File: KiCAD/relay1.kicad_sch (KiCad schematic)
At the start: 15 parts, among them K1 SANYOU_SRD_Form_C, K2 SANYOU_SRD_Form_C, Q2 UMH3N, Q3 MMBT3906, Q4 MMBT3906

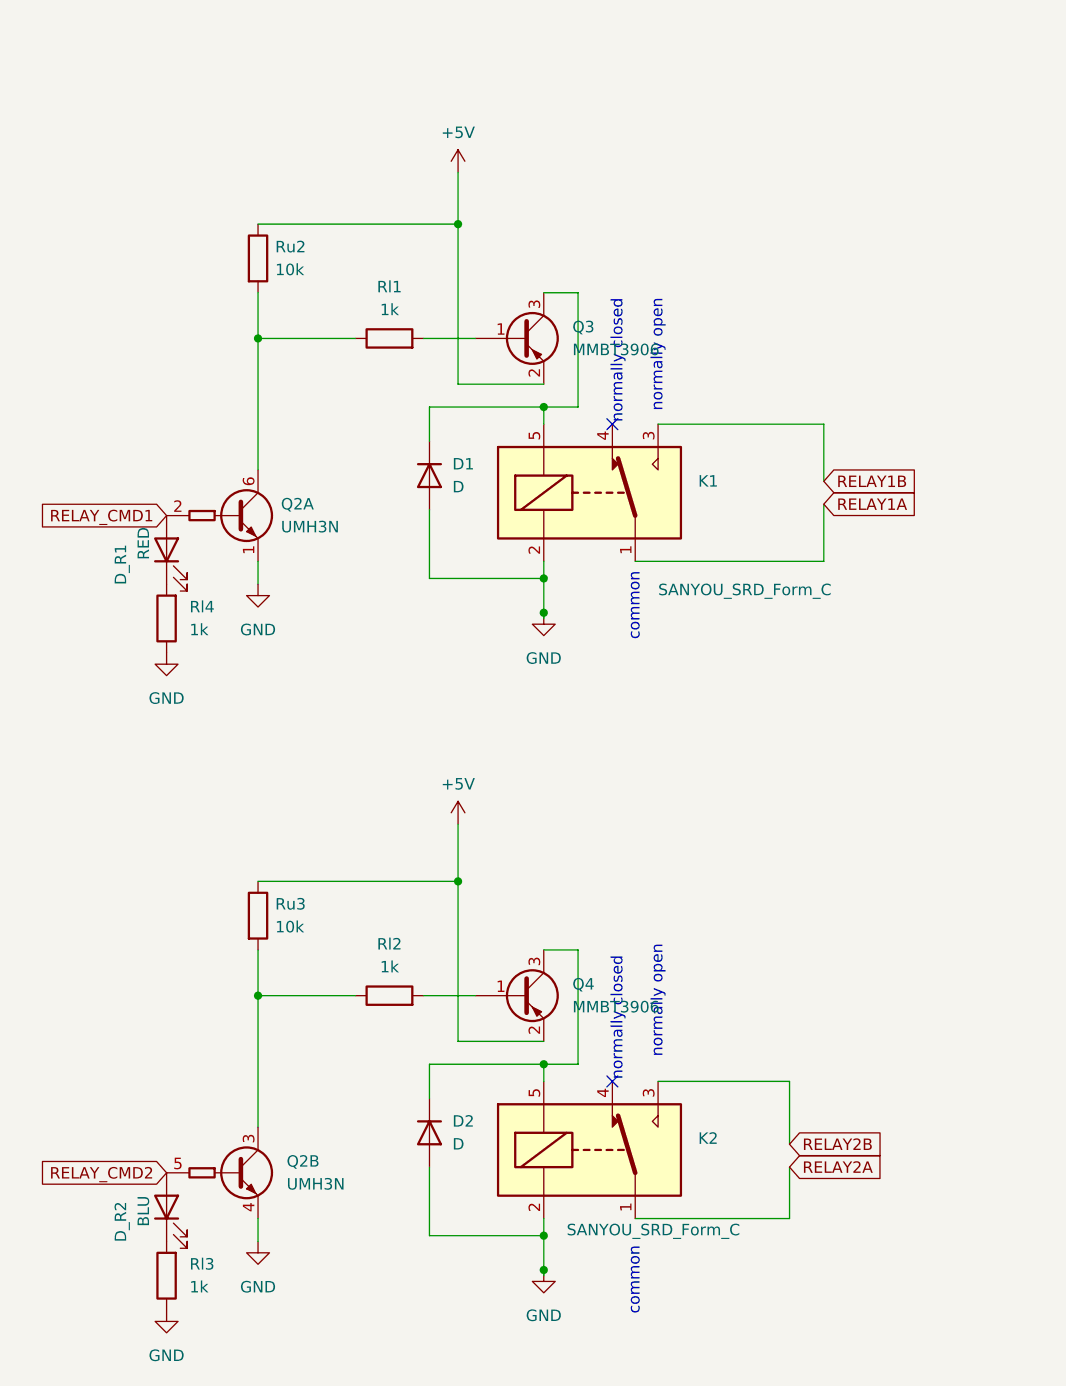
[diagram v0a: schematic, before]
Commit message: four-sonar board (#25)
The four-sonar board written about in [Dual Sonar ESP32 Garage State
Estimation](https://selectiveappeal.org/posts/garage133-dual-sonar/).

- Board supports front and back sonars for both right and left garage
bays.
- Software update for dual-observation hmm, training update.
  - Distinct states for door open with car present and not present.
- Updated ebox design, sencil fixture
- Updated device web interface
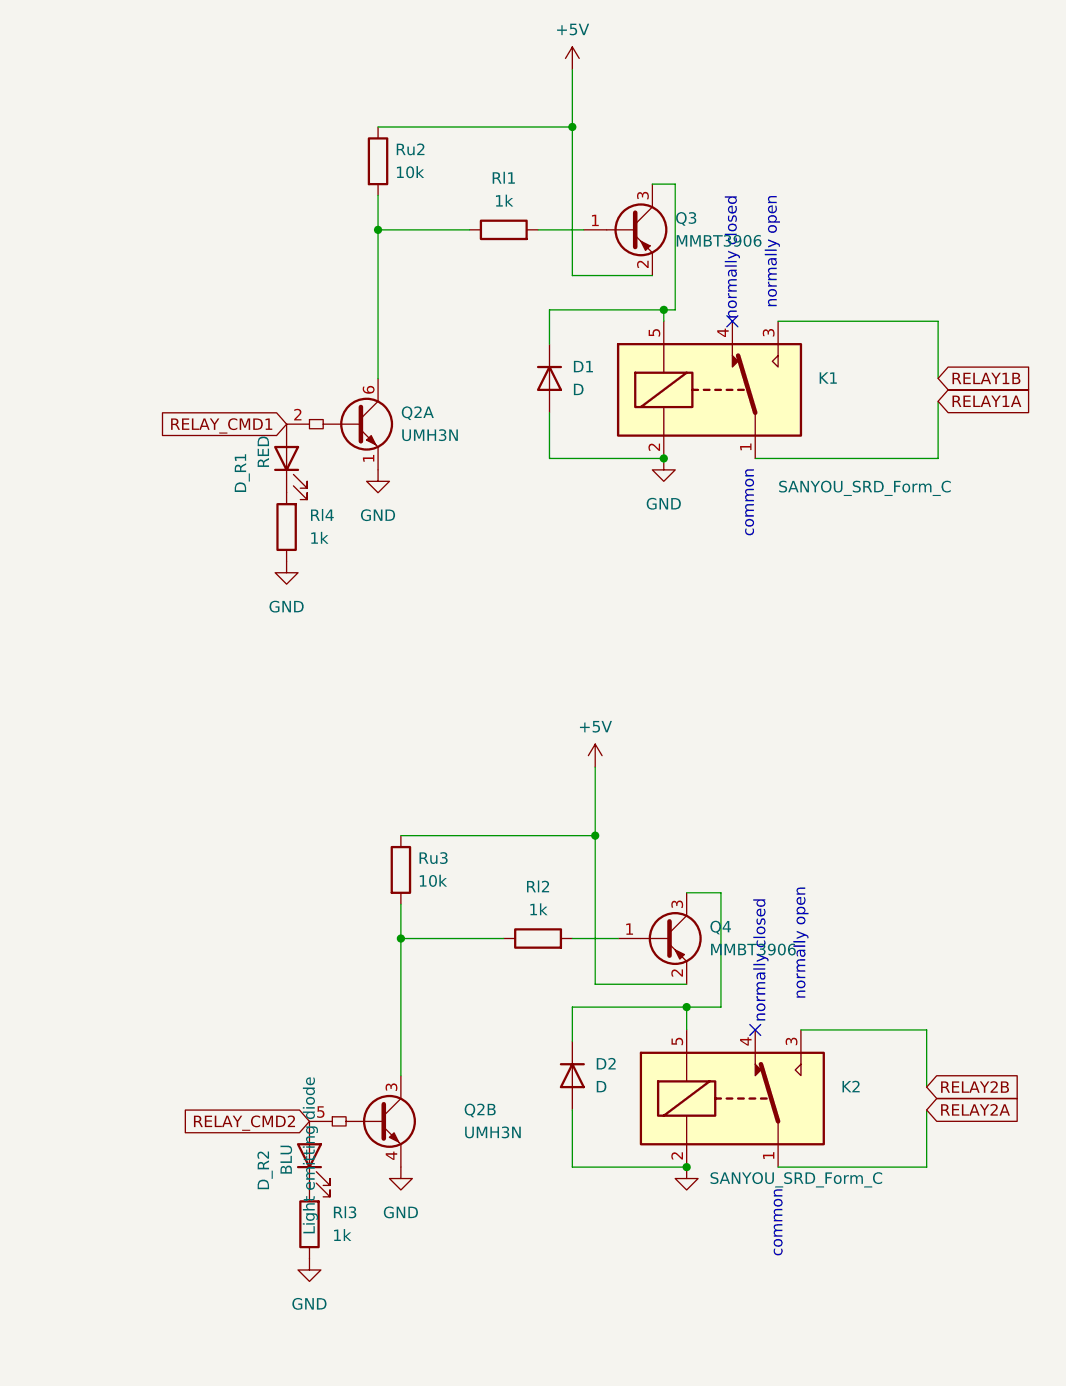
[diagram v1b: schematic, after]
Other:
- moved on the sheet: D1, D2, D_R1, D_R2, K1, K2, Q2A, Q2B, Rl1, Rl2, Rl3, Rl4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

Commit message: KiCAD board v3.0 changes (I think)
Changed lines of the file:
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@@
 	(text "normally closed"
 		(exclude_from_sim no)
-		(at 99.06 137.795 90)
+		(at 95.758 57.15 90)
 		(effects
 			(font
@@
 	(text "normally open"
 		(exclude_from_sim no)
-		(at 103.505 135.255 90)
-		(effects
-			(font
-				(size 1.27 1.27)
-			)
-			(justify left bottom)
-		)
-	)
-	(text "normally closed"
-		(exclude_from_sim no)
-		(at 95.885 59.69 90)
-		(effects
-			(font
-				(size 1.27 1.27)
-			)
-			(justify left bottom)
-		)
-	)
-	(text "normally open"
-		(exclude_from_sim no)
 		(at 100.33 58.42 90)
-		(effects
-			(font
-				(size 1.27 1.27)
-			)
-			(justify left bottom)
-		)
-	)
-	(text "common\n"
-		(exclude_from_sim no)
-		(at 100.965 163.83 90)
 		(effects
 			(font
@@
 		(dnp no)
 		(fields_autoplaced yes)
-		(property "Reference" "#PWR026"
+		(property "Reference" "#PWR0102"
 			(at 80.01 113.03 0)
 			(effects
@@
 			(project "Garage133"
 				(path "/42347524-93c6-40af-953e-da6b7c7bdf56/d90cc7d4-8419-4d79-8cad-11316efa8615"
-					(reference "#PWR026")
+					(reference "#PWR0102")
 					(unit 1)
 				)
@@
 			)
 		)
-		(property "Description" ""
+		(property "Description" "Sanyo SRD relay, Single Pole Miniature Power Relay,"
 			(at 95.25 146.05 0)
 			(effects
@@
 					(size 1.27 1.27)
 				)
+				(hide yes)
 			)
 		)
@@
 			)
 		)
-		(property "Description" ""
+		(property "Description" "Resistor"
 			(at 69.85 49.53 0)
 			(effects
@@
 					(size 1.27 1.27)
 				)
+				(hide yes)
 			)
 		)
@@
 			)
 		)
-		(property "Description" ""
+		(property "Description" "Sanyo SRD relay, Single Pole Miniature Power Relay,"
 			(at 92.71 67.31 0)
 			(effects
@@
 					(size 1.27 1.27)
 				)
+				(hide yes)
 			)
 		)
@@
 			)
 		)
-		(property "Description" ""
+		(property "Description" "Resistor"
 			(at 55.88 41.91 0)
 			(effects
@@
 					(size 1.27 1.27)
 				)
+				(hide yes)
 			)
 		)
@@
 		(on_board yes)
 		(dnp no)
-		(fields_autoplaced yes)
 		(property "Reference" "Q3"
 			(at 88.9 48.2599 0)
@@
 		)
 		(property "Value" "MMBT3906"
-			(at 88.9 50.7999 0)
+			(at 90.678 46.482 90)
 			(effects
 				(font
@@
 			)
 		)
-		(property "Description" ""
+		(property "Description" "Resistor"
 			(at 58.42 120.65 0)
 			(effects
@@
 			)
 		)
-		(property "Description" ""
+		(property "Description" "Resistor"
 			(at 45.72 82.55 0)
 			(effects
@@
 					(size 1.27 1.27)
 				)
+				(hide yes)
 			)
 		)
@@
 		(dnp no)
 		(fields_autoplaced yes)
-		(property "Reference" "#PWR023"
+		(property "Reference" "#PWR0101"
 			(at 77.47 35.56 0)
 			(effects
@@
 			(project "Garage133"
 				(path "/42347524-93c6-40af-953e-da6b7c7bdf56/d90cc7d4-8419-4d79-8cad-11316efa8615"
-					(reference "#PWR023")
+					(reference "#PWR0101")
 					(unit 1)
 				)
@@
 			)
 		)
-		(property "Description" ""
+		(property "Description" "Resistor"
 			(at 73.66 128.27 0)
 			(effects
@@
 					(size 1.27 1.27)
 				)
+				(hide yes)
 			)
 		)
@@
 			)
 		)
-		(property "Description" ""
+		(property "Description" "Diode"
 			(at 74.93 66.04 0)
 			(effects
@@
 					(size 1.27 1.27)
 				)
+				(hide yes)
 			)
 		)
@@
 			)
 		)
-		(property "Description" ""
+		(property "Description" "Resistor"
 			(at 48.26 160.02 0)
 			(effects
@@
 					(size 1.27 1.27)
 				)
+				(hide yes)
 			)
 		)
@@
 			)
 		)
-		(property "Description" ""
+		(property "Description" "Diode"
 			(at 77.47 143.51 0)
 			(effects
@@
 					(size 1.27 1.27)
 				)
-			)
-		)
+				(hide yes)
+			)
+		)

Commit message: PCB updates: board v3.1
- USB-C connect other side D+,D-
- Move USB-C to stick-out from board
- Push buttons for EN and PROG
- Move connectors away from OLED
- Move SHTC3 away from ESP32, to far side of relays. Thermal isolation milling.
- M2.5 hole for OLED support.
- Replace MMBT3906 transistors with MMBT4403 on Gemini recommendation.
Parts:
- D1, D2: value D -> B5817WS-TP
- Q3, Q4: value MMBT3906 -> MMBT4403
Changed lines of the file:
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@@
 			)
 		)
-		(property "Value" "MMBT3906"
+		(property "Value" "MMBT4403"
 			(at 92.71 129.5399 0)
 			(effects
@@
 			)
 		)
-		(property "Value" "MMBT3906"
+		(property "Value" "MMBT4403"
 			(at 90.678 46.482 90)
 			(effects
@@
 		(on_board yes)
 		(dnp no)
-		(fields_autoplaced yes)
 		(property "Reference" "D1"
 			(at 77.47 64.77 90)
@@
 			)
 		)
-		(property "Value" "D"
-			(at 77.47 67.31 90)
+		(property "Value" "B5817WS-TP"
+			(at 72.39 59.944 0)
 			(effects
 				(font
@@
 		(on_board yes)
 		(dnp no)
-		(fields_autoplaced yes)
 		(property "Reference" "D2"
 			(at 80.01 142.24 90)
@@
 			)
 		)
-		(property "Value" "D"
-			(at 80.01 144.78 90)
-			(effects
-				(font
+		(property "Value" "B5817WS-TP"
+			(at 74.93 136.906 0)
+			(effects
+				(font
